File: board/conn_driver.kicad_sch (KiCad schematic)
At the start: 5 parts, among them J13 Conn_02x07_Odd_Even, J14 Conn_01x02_Pin, J15 Conn_01x02_Pin, U13 HEF4093B

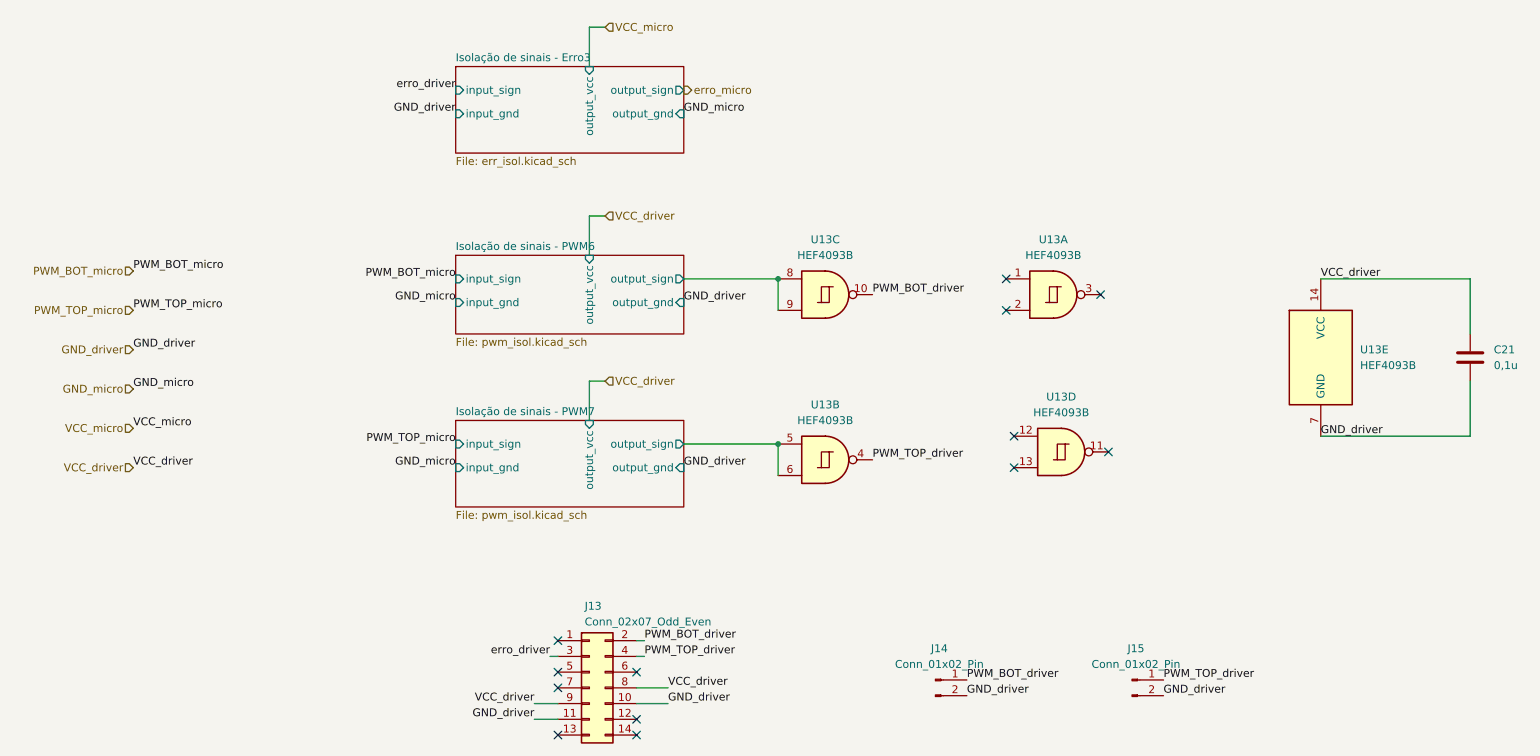
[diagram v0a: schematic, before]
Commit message: Finalização da placa, trilhas, planos de terra e footprint TJA1050
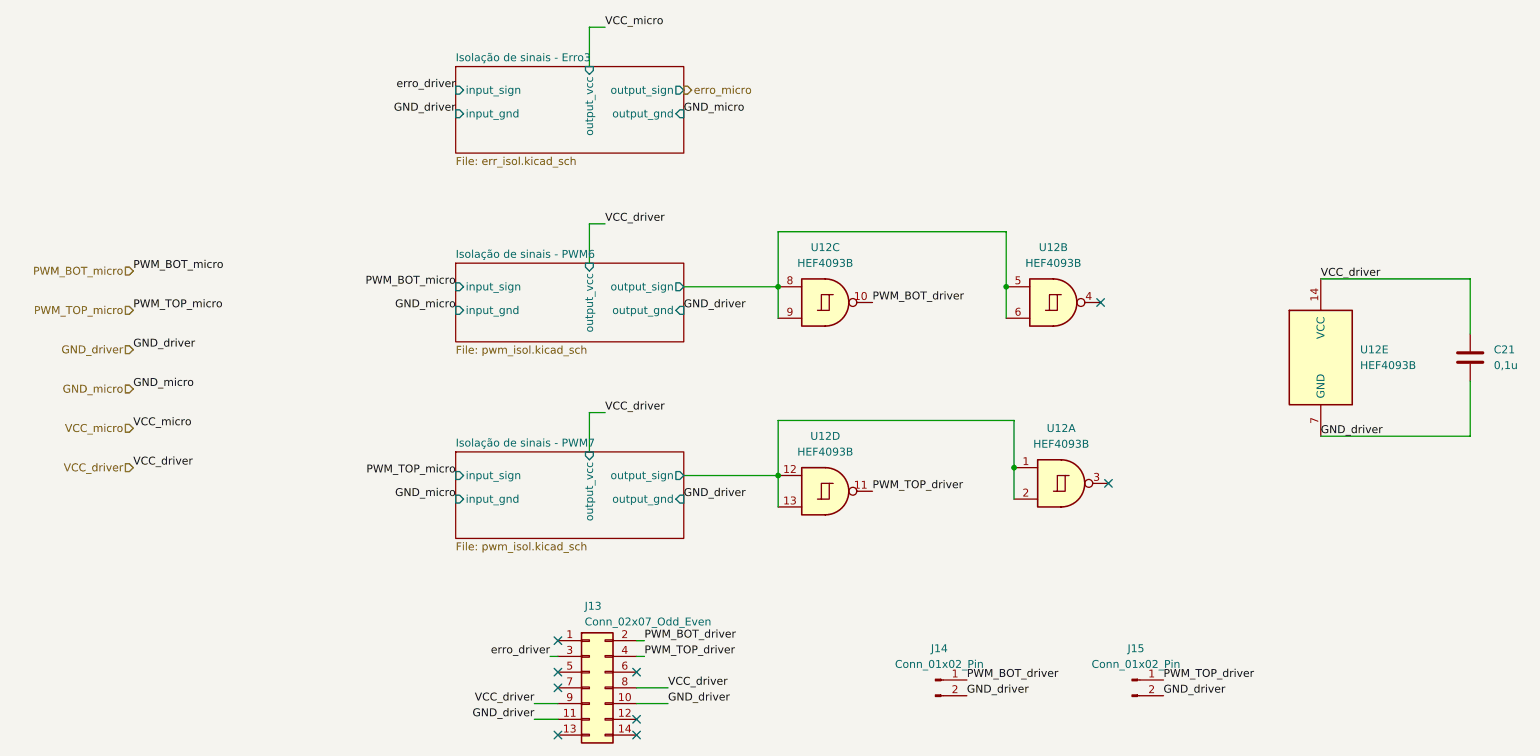
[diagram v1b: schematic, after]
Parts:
- renumbered U13 to U12
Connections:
- net Isolação de sinais - PWM6/output_sign: now also U12.5, U12.6
- net Isolação de sinais - PWM7/output_sign: now also U12.1, U12.12, U12.13, U12.2; no longer U12.5, U12.6
- net PWM_TOP_driver: now also U12.11; no longer U12.4
- no-connect marks 13 -> 9
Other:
- moved on the sheet: U12A, U12B, U12C, U12D

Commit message: Criação da placa de alimentação
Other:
- company: (none) -> Escola Politécnica da Universidade de São Paulo
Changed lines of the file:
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@@
 	(generator_version "8.0")
 	(paper "A4")
+	(title_block
+		(date "2025-10-02")
+		(company "Escola Politécnica da Universidade de São Paulo")
+	)
 	(junction
 		(at 140.97 72.39)
